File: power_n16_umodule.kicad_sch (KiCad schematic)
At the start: 25 parts, among them J1 LSHM-140-04.0-L-DV-A-N-K-TR, U1 LTM4651

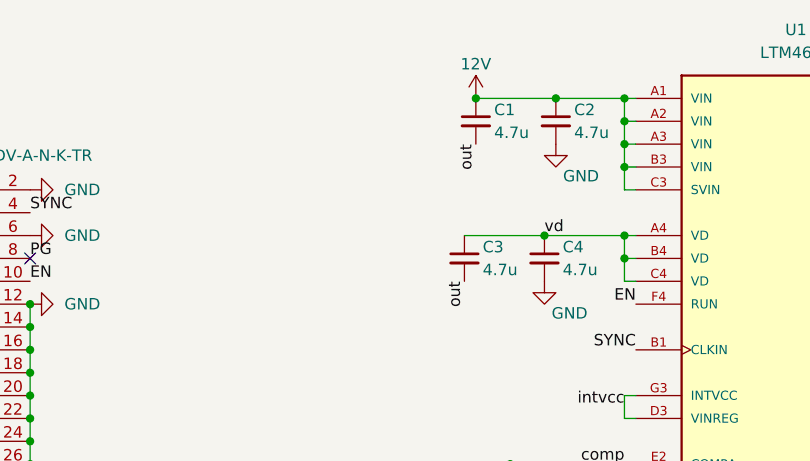
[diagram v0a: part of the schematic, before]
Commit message: Add Ferrite Beads
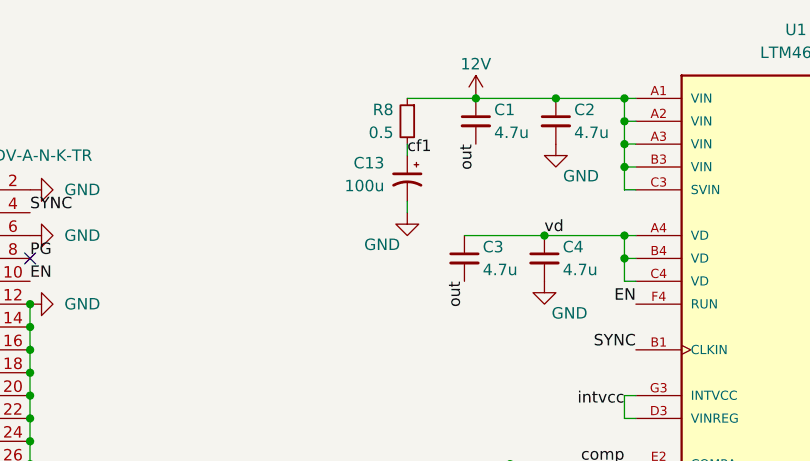
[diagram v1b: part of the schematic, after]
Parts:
- added C13: 100u, lib:T521X, symbol Device:C_Polarized_Small_US
- added R8: 0.5, Resistor_SMD:R_0603_1608Metric, symbol Device:R_Small
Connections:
- net 12V: now also R8.1
- net GND: now also C13.2
- new net cf1: C13.1, R8.2
